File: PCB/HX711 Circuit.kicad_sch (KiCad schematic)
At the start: 6 parts

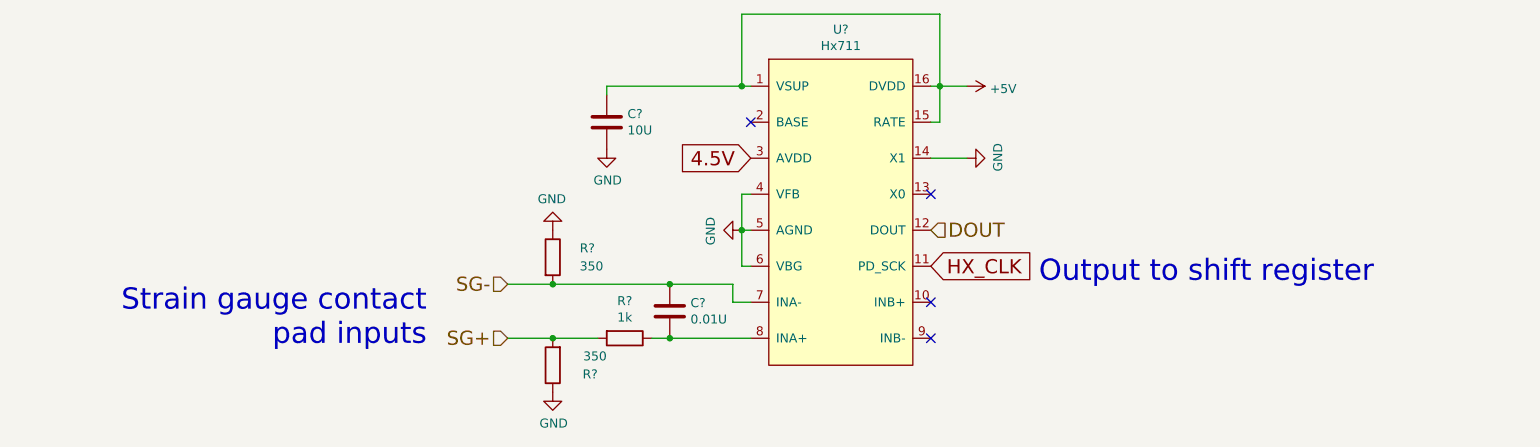
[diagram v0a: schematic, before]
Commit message: Swap shift registers. Start board layout
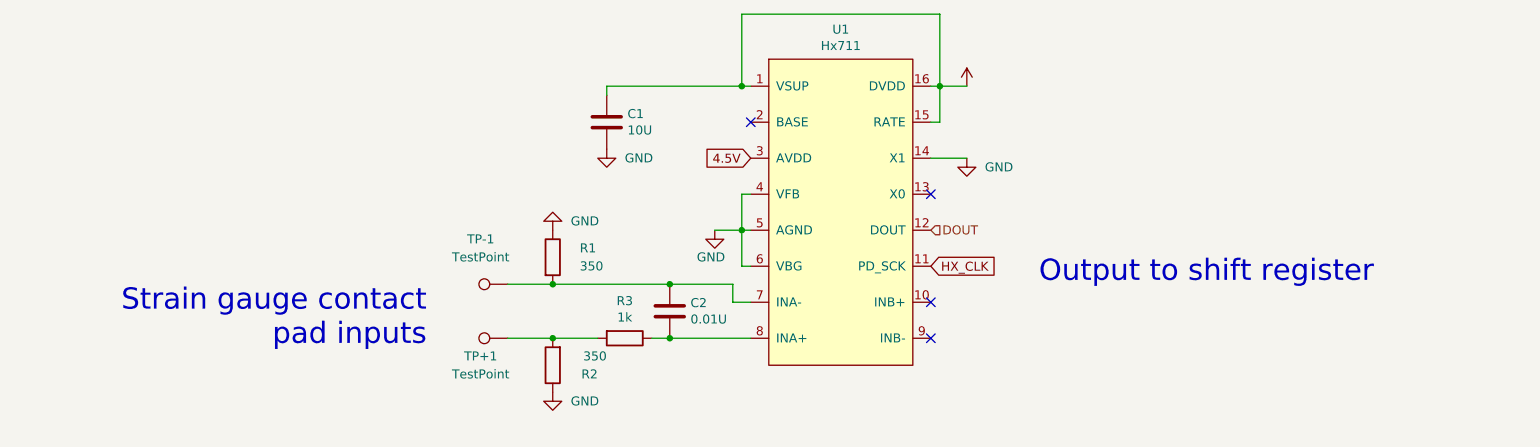
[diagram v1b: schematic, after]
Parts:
- added TP+1, TP-1: TestPoint, symbol Connector:TestPoint
- gave numbers to parts that had none: 6
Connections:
- net SG+: no longer names the net of R2.2, R3.2
- net SG+: now also TP+1.1
- net SG-: no longer names the net of C2.1, R1.2, U1.7 (INA-)
- net SG-: now also TP-1.1

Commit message: Start radial layout
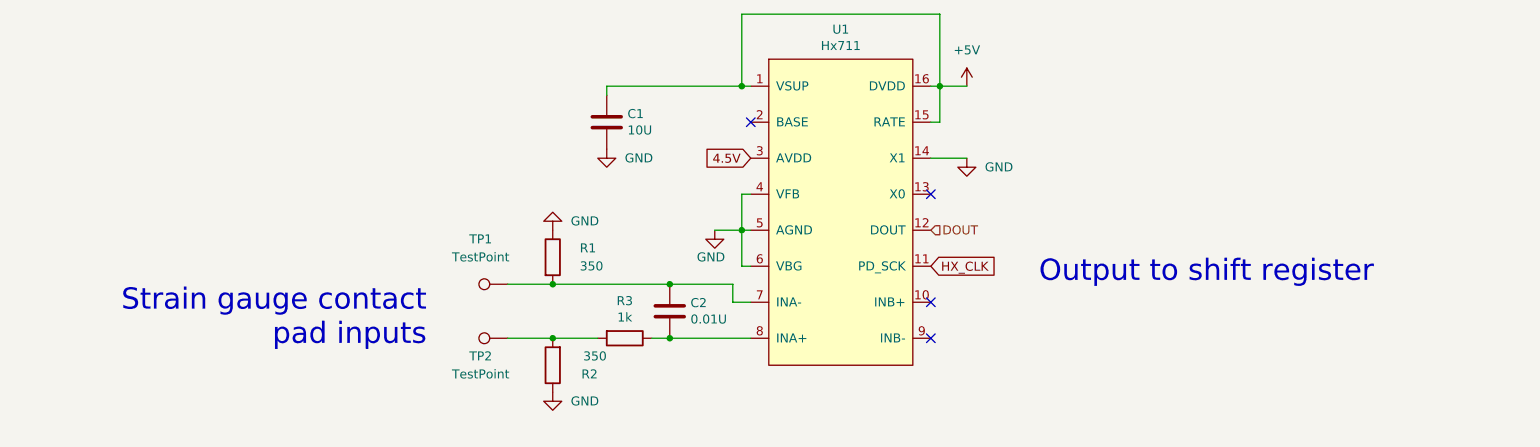
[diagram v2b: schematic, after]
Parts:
- TP1: renamed from TP-1; footprint (none) -> Custom-footprints:Radial-Pads-With-Relief
- TP2: renamed from TP+1; footprint (none) -> Custom-footprints:Radial-Pads-With-Relief
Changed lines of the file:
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@@
       (effects (font (size 1.27 1.27)) hide)
     )
-    (property "Value" "" (id 1) (at 172.72 71.12 0))
+    (property "Value" "+5V" (id 1) (at 172.72 71.12 0))
     (property "Footprint" "" (id 2) (at 172.72 76.2 0)
       (effects (font (size 1.27 1.27)) hide)
@@
   (symbol (lib_id "Connector:TestPoint") (at 107.95 111.76 90) (unit 1)
     (in_bom yes) (on_board yes)
-    (property "Reference" "TP+1" (id 0) (at 104.14 114.3 90))
+    (property "Reference" "TP2" (id 0) (at 104.14 114.3 90))
     (property "Value" "TestPoint" (id 1) (at 104.14 116.84 90))
-    (property "Footprint" "" (id 2) (at 107.95 106.68 0)
+    (property "Footprint" "Custom-footprints:Radial-Pads-With-Relief" (id 2) (at 107.95 106.68 0)
       (effects (font (size 1.27 1.27)) hide)
     )
@@
   (symbol (lib_id "Connector:TestPoint") (at 107.95 104.14 90) (unit 1)
     (in_bom yes) (on_board yes)
-    (property "Reference" "TP-1" (id 0) (at 104.14 97.79 90))
+    (property "Reference" "TP1" (id 0) (at 104.14 97.79 90))
     (property "Value" "TestPoint" (id 1) (at 104.14 100.33 90))
-    (property "Footprint" "" (id 2) (at 107.95 99.06 0)
+    (property "Footprint" "Custom-footprints:Radial-Pads-With-Relief" (id 2) (at 107.95 99.06 0)
       (effects (font (size 1.27 1.27)) hide)
     )

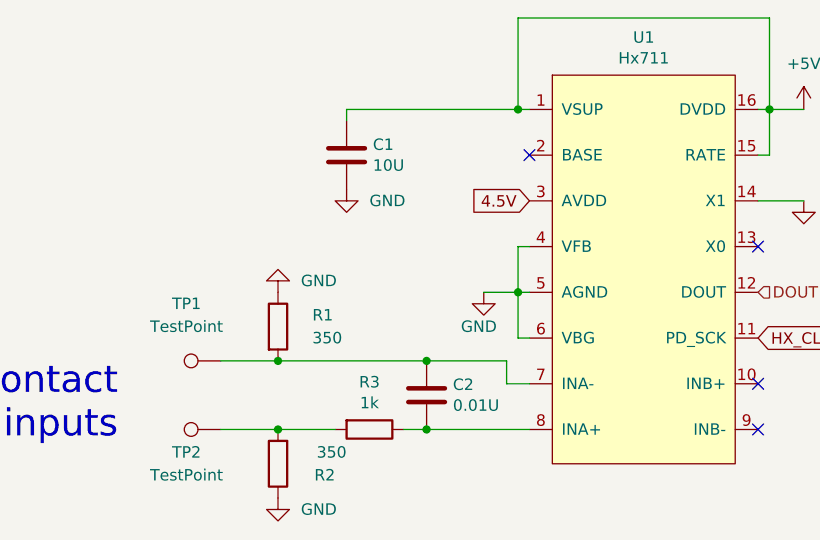
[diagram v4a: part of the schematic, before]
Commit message: Add second decoupling cap to HXs
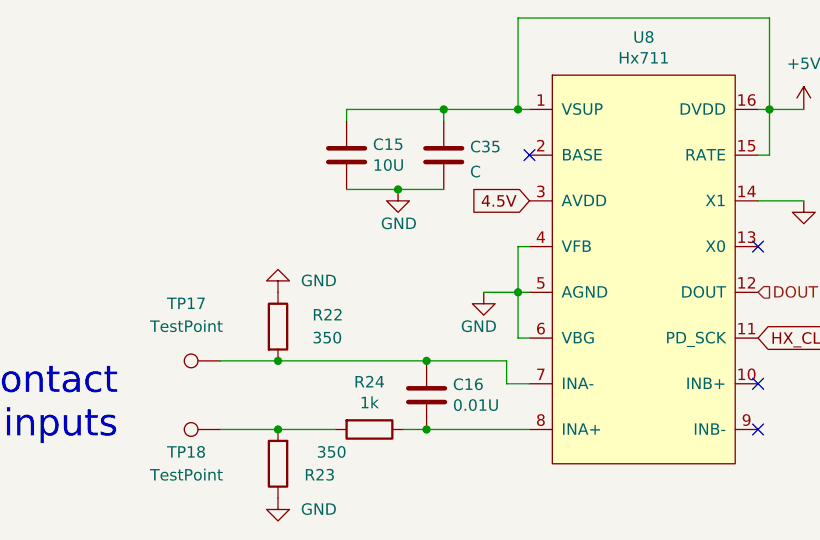
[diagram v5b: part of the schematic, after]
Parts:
- added C35: C, symbol Device:C
- renumbered C1 to C15, C2 to C16, R1 to R22, R2 to R23, R3 to R24, TP1 to TP17, TP2 to TP18, U1 to U8
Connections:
- net +5V: now also C35.1
- net GND: now also C35.2
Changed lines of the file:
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@@
   (junction (at 130.81 104.14) (diameter 0) (color 0 0 0 0)
   )
+  (junction (at 132.715 76.2) (diameter 0) (color 0 0 0 0)
+  )
   (junction (at 114.3 104.14) (diameter 0) (color 0 0 0 0)
   )
@@
   )
   (junction (at 130.81 111.76) (diameter 0) (color 0 0 0 0)
+  )
+  (junction (at 127.635 85.09) (diameter 0) (color 0 0 0 0)
   )
   (junction (at 114.3 111.76) (diameter 0) (color 0 0 0 0)
@@
     (stroke (width 0) (type default) (color 0 0 0 0))
   )
+  (wire (pts (xy 132.715 76.2) (xy 132.715 77.47))
+    (stroke (width 0) (type default) (color 0 0 0 0))
+  )
   (wire (pts (xy 139.7 104.14) (xy 130.81 104.14))
     (stroke (width 0) (type default) (color 0 0 0 0))
@@
     (stroke (width 0) (type default) (color 0 0 0 0))
   )
+  (wire (pts (xy 132.715 76.2) (xy 140.97 76.2))
+    (stroke (width 0) (type default) (color 0 0 0 0))
+  )
   (wire (pts (xy 107.95 111.76) (xy 114.3 111.76))
     (stroke (width 0) (type default) (color 0 0 0 0))
@@
     (stroke (width 0) (type default) (color 0 0 0 0))
   )
+  (wire (pts (xy 121.92 85.09) (xy 127.635 85.09))
+    (stroke (width 0) (type default) (color 0 0 0 0))
+  )
   (wire (pts (xy 168.91 66.04) (xy 168.91 76.2))
     (stroke (width 0) (type default) (color 0 0 0 0))
@@
     (stroke (width 0) (type default) (color 0 0 0 0))
   )
-  (wire (pts (xy 121.92 76.2) (xy 140.97 76.2))
+  (wire (pts (xy 127.635 85.09) (xy 132.715 85.09))
+    (stroke (width 0) (type default) (color 0 0 0 0))
+  )
+  (wire (pts (xy 121.92 76.2) (xy 132.715 76.2))
     (stroke (width 0) (type default) (color 0 0 0 0))
   )
@@
     (effects (font (size 1.27 1.27)) (justify left))
   )
-  (symbol (lib_id "PCB-rescue:C-Device") (at 121.92 81.28 0) (unit 1)
-    (in_bom yes) (on_board yes)
-    (property "Reference" "C1" (id 0) (at 124.841 80.1116 0)
+  (symbol (lib_id "PCB-rescue:C-Device") (at 121.92 81.28 0)
+    (in_bom yes) (on_board yes)
+    (property "Reference" "C15" (id 0) (at 124.841 80.1116 0)
       (effects (font (size 1.27 1.27)) (justify left))
     )
@@
     (pin "2")
   )
-  (symbol (lib_id "power:GND") (at 114.3 119.38 0) (unit 1)
-    (in_bom yes) (on_board yes) (fields_autoplaced)
-    (property "Reference" "#PWR0103" (id 0) (at 114.3 125.73 0)
+  (symbol (lib_id "Device:C") (at 132.715 81.28 0)
+    (in_bom yes) (on_board yes) (fields_autoplaced)
+    (property "Reference" "C35" (id 0) (at 135.636 80.3715 0)
+      (effects (font (size 1.27 1.27)) (justify left))
+    )
+    (property "Value" "C" (id 1) (at 135.636 83.1466 0)
+      (effects (font (size 1.27 1.27)) (justify left))
+    )
+    (property "Footprint" "" (id 2) (at 133.6802 85.09 0)
+      (effects (font (size 1.27 1.27)) hide)
+    )
+    (property "Datasheet" "~" (id 3) (at 132.715 81.28 0)
+      (effects (font (size 1.27 1.27)) hide)
+    )
+    (pin "1")
+    (pin "2")
+  )
+  (symbol (lib_id "power:GND") (at 114.3 119.38 0)
+    (in_bom yes) (on_board yes) (fields_autoplaced)
+    (property "Reference" "#PWR0139" (id 0) (at 114.3 125.73 0)
       (effects (font (size 1.27 1.27)) hide)
     )
@@
     (pin "1")
   )
-  (symbol (lib_id "power:GND") (at 121.92 85.09 0) (unit 1)
-    (in_bom yes) (on_board yes) (fields_autoplaced)
-    (property "Reference" "#PWR0104" (id 0) (at 121.92 91.44 0)
-      (effects (font (size 1.27 1.27)) hide)
-    )
-    (property "Value" "GND" (id 1) (at 124.46 86.3599 0)
-      (effects (font (size 1.27 1.27)) (justify left))
-    )
-    (property "Footprint" "" (id 2) (at 121.92 85.09 0)
-      (effects (font (size 1.27 1.27)) hide)
-    )
-    (property "Datasheet" "" (id 3) (at 121.92 85.09 0)
-      (effects (font (size 1.27 1.27)) hide)
-    )
-    (pin "1")
-  )
-  (symbol (lib_id "power:GND") (at 137.16 96.52 0) (unit 1)
-    (in_bom yes) (on_board yes)
-    (property "Reference" "#PWR0106" (id 0) (at 137.16 102.87 0)
+  (symbol (lib_id "power:GND") (at 127.635 85.09 0)
+    (in_bom yes) (on_board yes)
+    (property "Reference" "#PWR0140" (id 0) (at 127.635 91.44 0)
+      (effects (font (size 1.27 1.27)) hide)
+    )
+    (property "Value" "GND" (id 1) (at 125.73 88.9 0)
+      (effects (font (size 1.27 1.27)) (justify left))
+    )
+    (property "Footprint" "" (id 2) (at 127.635 85.09 0)
+      (effects (font (size 1.27 1.27)) hide)
+    )
+    (property "Datasheet" "" (id 3) (at 127.635 85.09 0)
+      (effects (font (size 1.27 1.27)) hide)
+    )
+    (pin "1")
+  )
+  (symbol (lib_id "power:GND") (at 137.16 96.52 0)
+    (in_bom yes) (on_board yes)
+    (property "Reference" "#PWR0142" (id 0) (at 137.16 102.87 0)
       (effects (font (size 1.27 1.27)) hide)
     )
@@
     (pin "1")
   )
-  (symbol (lib_id "power:+5V") (at 172.72 76.2 0) (unit 1)
-    (in_bom yes) (on_board yes) (fields_autoplaced)
-    (property "Reference" "#PWR0101" (id 0) (at 172.72 80.01 0)
+  (symbol (lib_id "power:+5V") (at 172.72 76.2 0)
+    (in_bom yes) (on_board yes) (fields_autoplaced)
+    (property "Reference" "#PWR0137" (id 0) (at 172.72 80.01 0)
       (effects (font (size 1.27 1.27)) hide)
     )
@@
     (pin "1")
   )
-  (symbol (lib_id "power:GND") (at 114.3 96.52 180) (unit 1)
-    (in_bom yes) (on_board yes) (fields_autoplaced)
-    (property "Reference" "#PWR0105" (id 0) (at 114.3 90.17 0)
+  (symbol (lib_id "power:GND") (at 114.3 96.52 180)
+    (in_bom yes) (on_board yes) (fields_autoplaced)
+    (property "Reference" "#PWR0141" (id 0) (at 114.3 90.17 0)
       (effects (font (size 1.27 1.27)) hide)
     )
@@
     (pin "1")
   )
-  (symbol (lib_id "Connector:TestPoint") (at 107.95 111.76 90) (unit 1)
-    (in_bom yes) (on_board yes)
-    (property "Reference" "TP2" (id 0) (at 104.14 114.3 90))
+  (symbol (lib_id "Connector:TestPoint") (at 107.95 111.76 90)
+    (in_bom yes) (on_board yes)
+    (property "Reference" "TP18" (id 0) (at 104.14 114.3 90))
     (property "Value" "TestPoint" (id 1) (at 104.14 116.84 90))
     (property "Footprint" "Custom-footprints:Radial-Pads-With-Relief" (id 2) (at 107.95 106.68 0)
@@
     (pin "1")
   )
-  (symbol (lib_id "Device:R") (at 114.3 100.33 0) (unit 1)
-    (in_bom yes) (on_board yes) (fields_autoplaced)
-    (property "Reference" "R1" (id 0) (at 118.11 99.0599 0)
+  (symbol (lib_id "Device:R") (at 114.3 100.33 0)
+    (in_bom yes) (on_board yes) (fields_autoplaced)
+    (property "Reference" "R22" (id 0) (at 118.11 99.0599 0)
       (effects (font (size 1.27 1.27)) (justify left))
     )
@@
     (pin "2")
   )
-  (symbol (lib_id "PCB-rescue:R-Device") (at 124.46 111.76 270) (unit 1)
-    (in_bom yes) (on_board yes)
-    (property "Reference" "R3" (id 0) (at 124.46 106.5022 90))
+  (symbol (lib_id "PCB-rescue:R-Device") (at 124.46 111.76 270)
+    (in_bom yes) (on_board yes)
+    (property "Reference" "R24" (id 0) (at 124.46 106.5022 90))
     (property "Value" "1k" (id 1) (at 124.46 108.8136 90))
     (property "Footprint" "Resistor_SMD:R_0805_2012Metric_Pad1.20x1.40mm_HandSolder" (id 2) (at 124.46 109.982 90)
@@
     (pin "2")
   )
-  (symbol (lib_id "power:GND") (at 172.72 86.36 0) (unit 1)
-    (in_bom yes) (on_board yes) (fields_autoplaced)
-    (property "Reference" "#PWR0102" (id 0) (at 172.72 92.71 0)
+  (symbol (lib_id "power:GND") (at 172.72 86.36 0)
+    (in_bom yes) (on_board yes) (fields_autoplaced)
+    (property "Reference" "#PWR0138" (id 0) (at 172.72 92.71 0)
       (effects (font (size 1.27 1.27)) hide)
     )
@@
     (pin "1")
   )
-  (symbol (lib_id "PCB-rescue:Hx711-HX711-HX711-ADC-rescue") (at 151.13 114.3 0) (unit 1)
-    (in_bom yes) (on_board yes)
-    (property "Reference" "U1" (id 0) (at 154.94 68.199 0))
+  (symbol (lib_id "PCB-rescue:Hx711-HX711-HX711-ADC-rescue") (at 151.13 114.3 0)
+    (in_bom yes) (on_board yes)
+    (property "Reference" "U8" (id 0) (at 154.94 68.199 0))
     (property "Value" "Hx711" (id 1) (at 154.94 70.5104 0))
     (property "Footprint" "Package_SO:SOIC-16_3.9x9.9mm_P1.27mm" (id 2) (at 154.94 63.5 0)
@@
     (pin "9")
   )
-  (symbol (lib_id "Connector:TestPoint") (at 107.95 104.14 90) (unit 1)
-    (in_bom yes) (on_board yes)
-    (property "Reference" "TP1" (id 0) (at 104.14 97.79 90))
+  (symbol (lib_id "Connector:TestPoint") (at 107.95 104.14 90)
+    (in_bom yes) (on_board yes)
+    (property "Reference" "TP17" (id 0) (at 104.14 97.79 90))
     (property "Value" "TestPoint" (id 1) (at 104.14 100.33 90))
     (property "Footprint" "Custom-footprints:Radial-Pads-With-Relief" (id 2) (at 107.95 99.06 0)
@@
     (pin "1")
   )
-  (symbol (lib_id "Device:R") (at 114.3 115.57 180) (unit 1)
-    (in_bom yes) (on_board yes)
-    (property "Reference" "R2" (id 0) (at 120.65 116.84 0)
+  (symbol (lib_id "Device:R") (at 114.3 115.57 180)
+    (in_bom yes) (on_board yes)
+    (property "Reference" "R23" (id 0) (at 120.65 116.84 0)
       (effects (font (size 1.27 1.27)) (justify left))
     )
@@
     (pin "2")
   )
-  (symbol (lib_id "PCB-rescue:C-Device") (at 130.81 107.95 0) (unit 1)
-    (in_bom yes) (on_board yes)
-    (property "Reference" "C2" (id 0) (at 133.731 106.7816 0)
-      (effects (font (size 1.27 1.27)) (justify left))
-    )
+  (symbol (lib_id "PCB-rescue:C-Device") (at 130.81 107.95 0)
+    (in_bom yes) (on_board yes)
+    (property "Reference" "C16" (id 0) (at 133.731 106.7816 0)
+      (effects (font (size 1.27 1.27)) (justify left))
+    )
